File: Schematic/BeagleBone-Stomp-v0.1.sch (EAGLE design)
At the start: 53 parts, among them U1 MSP430G2553_RHB_32, U2 TLV320AIC3120_RHB_32, U3 TPS73701_DRB_8

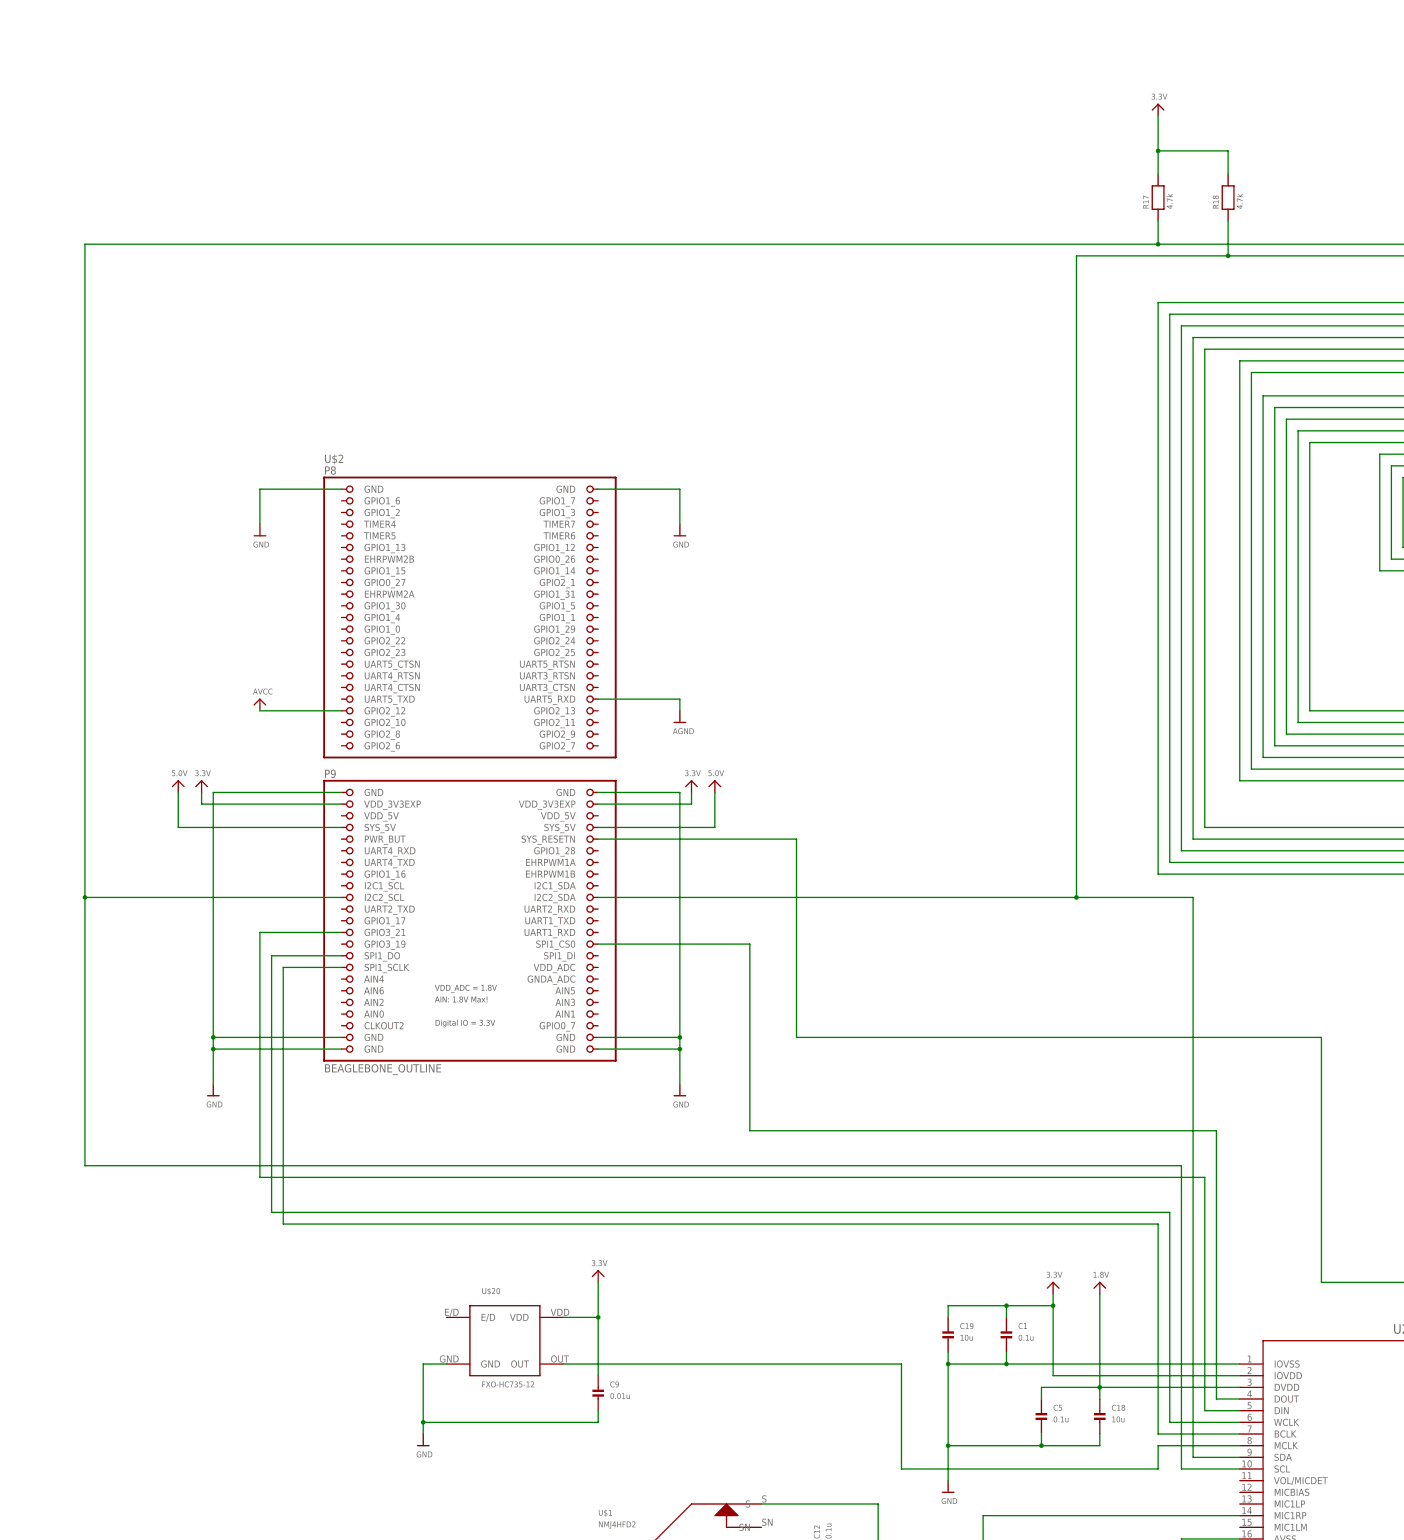
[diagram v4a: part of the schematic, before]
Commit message: Adding in EEPROM chip
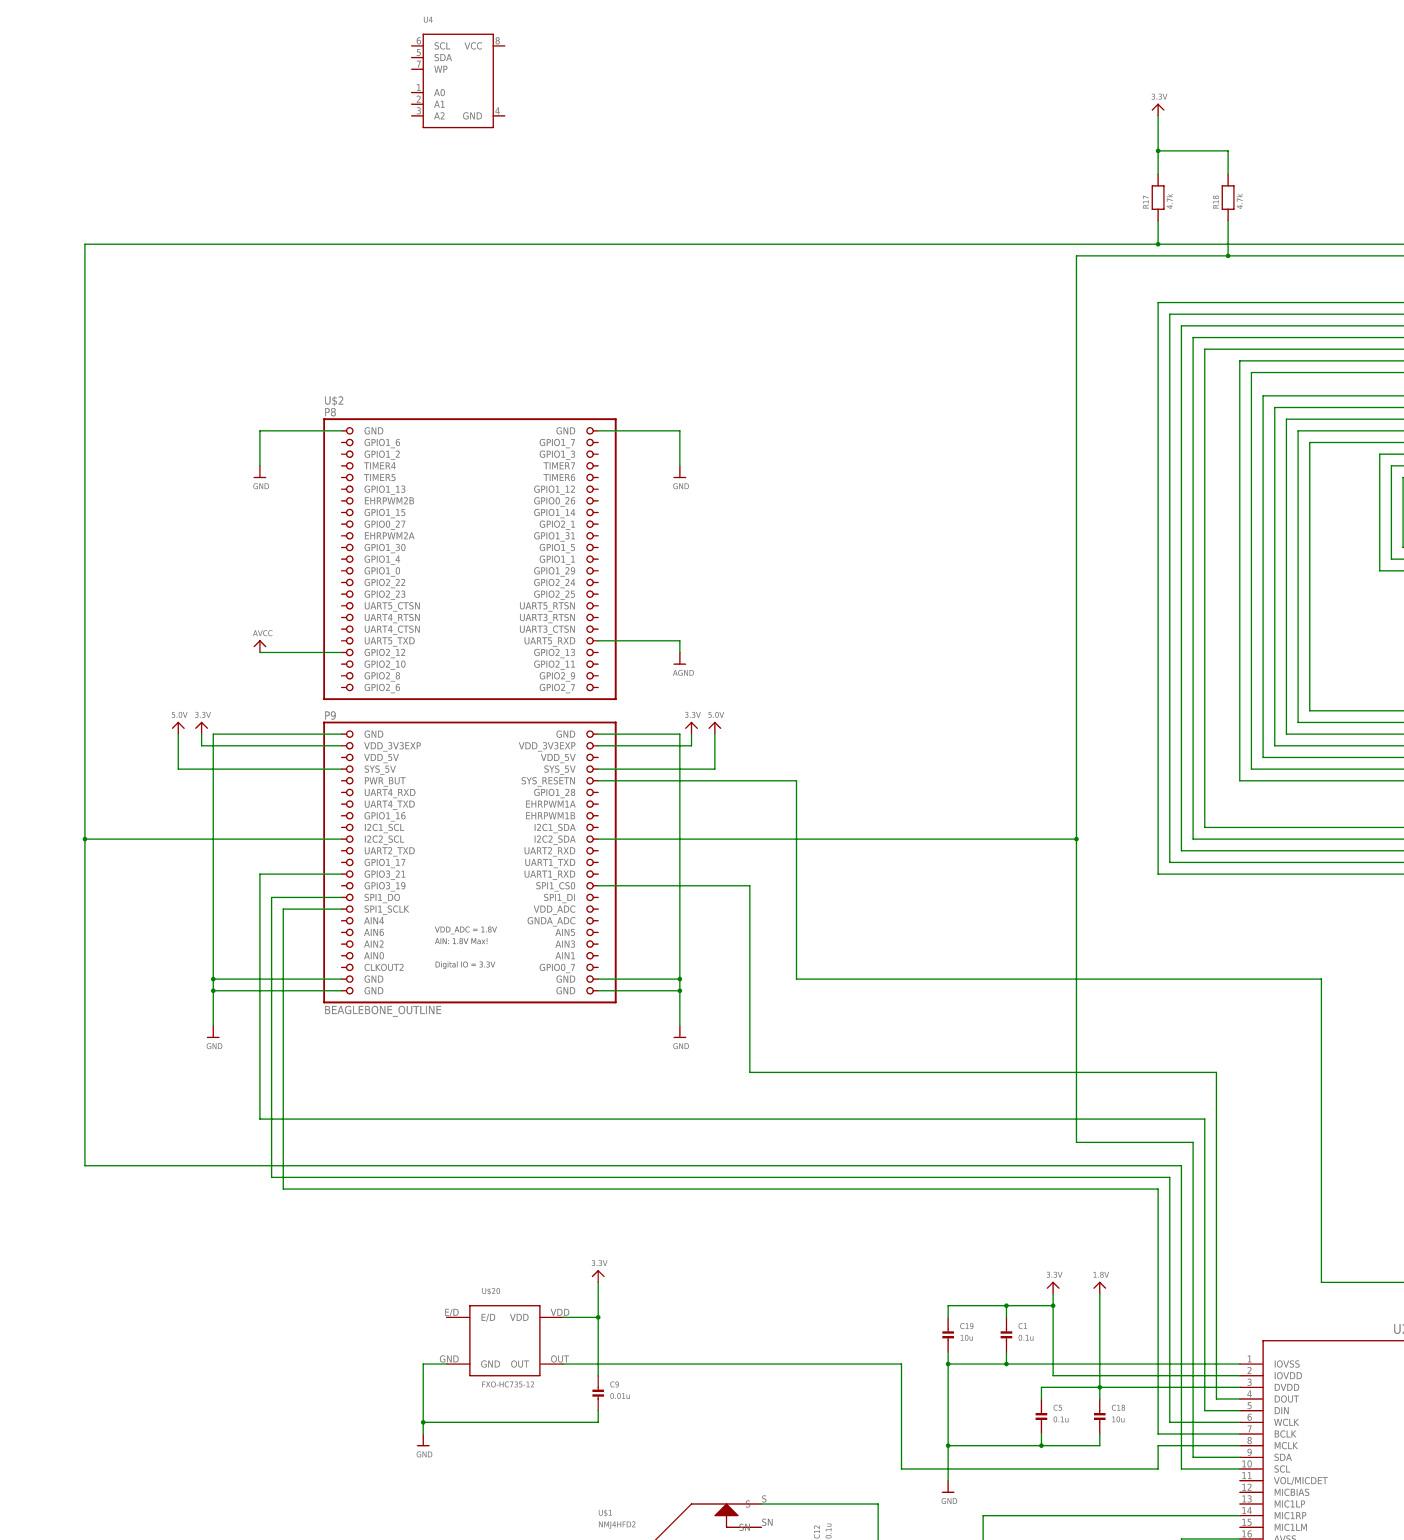
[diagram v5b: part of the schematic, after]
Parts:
- added U4: (no value), microbuilder:EEPROM_I2C_SOIC8_GENERIC
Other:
- moved on the sheet: U$2

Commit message: Pretty close to being done just need to check connections on schematic and make BOM
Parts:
- removed C13: 0.1u, microbuilder:CAP_CERAMIC0402
- added C11: 0.1u, microbuilder:CAP_CERAMIC0402
- added R19, R20, R21: 4.7k, microbuilder:RESISTOR0402
- added R22: 10k, microbuilder:RESISTOR0402
- added SW1: (no value), microbuilder:DIPSWITCH_2PIN
- R3, R4, R5, R6, R7, R8, R9: value 470 -> 100
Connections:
- removed net AVCC: U$2.GPIO2_12
- removed net N$17: JP2.1, U1.P1.5/TA0.0/UCB0CLK/UCA0STE/A5/CA5/TMS
- removed net N$19: JP2.4, U1.P1.2/TA0.1/UCA0TXD/UCA0SIMO/A2/CA2
- removed net N$20: JP2.5, U1.P1.1/TA0.0/UCA0RXD/UCA0SOMI/A1/CA1
- removed net N$21: JP2.3, U1.P1.3/ADC10CLK/CAOUT/VREF-/VEREF-/A3/CA3
- removed net N$24: U$2.GPIO3_21, U2.DIN
- removed net N$25: JP1.19, U1.P2.3/TA1.0
- removed net N$26: JP1.20, U1.P3.4/TA0.0
- removed net N$27: JP1.14, U1.P3.7/TA1CLK/CAOUT
- removed net N$28: JP1.15, U1.P3.6/TA0.2
- removed net N$29: JP1.16, U1.P3.5/TA0.1
- removed net N$30: JP1.17, U1.P2.5/TA1.2
- removed net N$31: JP1.18, U1.P2.4/TA1.2
- removed net N$34: JP2.7, R16.2, U1.P3.1/TA1.0
- removed net N$35: JP2.8, R15.2, U1.P3.0/TA0.2
- removed net N$36: JP2.9, R14.2, U1.P2.0/TA1.0
- removed net N$37: JP2.10, R13.2, U1.P2.1/TA1.1
- removed net N$38: JP2.11, R12.2, U1.P2.2/TA1.1
- removed net N$39: JP2.12, R11.2, U1.P3.2/TA1.1
- removed net N$40: JP2.13, R10.2, U1.P3.3/TA1.2
- removed net N$41: U$2.SPI1_DO, U2.WCLK
- removed net N$42: U$2.SPI1_SCLK, U2.BCLK
- removed net N$43: C16.P$1, C17.P$1, U2.SPKVDD_2
- removed net N$45: U$2.SYS_RESETN, U2.*RESET
- removed net N$46: R17.1, U$2.I2C2_SCL, U1.P1.6/TA0.1/UCB0SOMI/UCB0SCL/A6/CA6/TDI/TCLK, U2.SCL
- removed net N$47: R18.1, U$2.I2C2_SDA, U1.P1.7/CAOUT/UCB0SIMO/UCB0SDA/A7/CA7/TDO/TDI, U2.SDA
- removed net N$8 (its old number): U$20.OUT, U2.MCLK
- new net N$5: R19.1, SW1.1B, U4.A0
- new net P$1: JP1.14, JP1.15, JP1.16, JP1.17, JP1.18, JP1.19, JP1.20, JP2.1, JP2.10, JP2.11, JP2.12, JP2.13, JP2.2, JP2.3, JP2.4, JP2.5, JP2.6, JP2.7, JP2.8, JP2.9, R10.2, R11.2, R12.2, R13.2, R14.2, R15.2, R16.2, R17.1, R18.1, U$1.SN, U$1.TN, U$2.GPIO3_21, U$2.I2C2_SCL, U$2.I2C2_SDA, U$2.SPI1_CS0, U$2.SPI1_DO, U$2.SPI1_SCLK, U$2.SYS_RESETN, U$20.E/D, U$20.OUT, U$7.SN, U$7.TN, U1.NC, U1.NC_2, U1.P1.0/TA0CLK/ACLK/A0/CA0, U1.P1.1/TA0.0/UCA0RXD/UCA0SOMI/A1/CA1, U1.P1.2/TA0.1/UCA0TXD/UCA0SIMO/A2/CA2, U1.P1.3/ADC10CLK/CAOUT/VREF-/VEREF-/A3/CA3, U1.P1.4/SMCLK/UCB0STE/UCA0CLK/VREF+/VEREF+/A4/CA4/TCK, U1.P1.5/TA0.0/UCB0CLK/UCA0STE/A5/CA5/TMS, U1.P1.6/TA0.1/UCB0SOMI/UCB0SCL/A6/CA6/TDI/TCLK, U1.P1.7/CAOUT/UCB0SIMO/UCB0SDA/A7/CA7/TDO/TDI, U1.P2.0/TA1.0, U1.P2.1/TA1.1, U1.P2.2/TA1.1, U1.P2.3/TA1.0, U1.P2.4/TA1.2, U1.P2.5/TA1.2, U1.P3.0/TA0.2, U1.P3.1/TA1.0, U1.P3.2/TA1.1, U1.P3.3/TA1.2, U1.P3.4/TA0.0, U1.P3.5/TA0.1, U1.P3.6/TA0.2, U1.P3.7/TA1CLK/CAOUT, U1.XIN/P2.6/TA0.1, U1.XOUT/P2.7, U2.*RESET, U2.BCLK, U2.DIN, U2.DOUT, U2.GPIO1, U2.MCLK, U2.MIC1LM, U2.MIC1LP, U2.MICBIAS, U2.NC, U2.SCL, U2.SDA, U2.VOL/MICDET, U2.WCLK, U3.NC, U3.NC_2, U3.NC_3, U4.SCL, U4.SDA
- net 3.3V: now also C11.P$1, R19.2, R20.2, R21.2, R22.2, U4.VCC; no longer C13.P$1
- net 5.0V: now also C16.P$1, C17.P$1, U2.SPKVDD_2
- net AGND: no longer C13.P$2, U$2.UART5_RXD, U1.AVSS, U1.EPAD
- net GND: now also C11.P$2, SW1.1A, SW1.2A, U1.AVSS, U1.EPAD, U4.GND
- net N$11: now also R20.1, SW1.2B, U4.A1; no longer U$2.SPI1_CS0, U2.DOUT
- net N$12: now also R21.1, U4.A2; no longer JP2.6, U1.P1.0/TA0CLK/ACLK/A0/CA0
- net N$18: now also R22.1, U4.WP; no longer JP2.2, U1.P1.4/SMCLK/UCB0STE/UCA0CLK/VREF+/VEREF+/A4/CA4/TCK
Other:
- moved on the sheet: C1, C10, C12, C14, C15, C16, C17, C18, C19, C2, C3, C4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

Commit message: Removing arrows and such
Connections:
- removed net P$1: JP1.14, JP1.15, JP1.16, JP1.17, JP1.18, JP1.19, JP1.20, JP2.1, JP2.10, JP2.11, JP2.12, JP2.13, JP2.2, JP2.3, JP2.4, JP2.5, JP2.6, JP2.7, JP2.8, JP2.9, R10.2, R11.2, R12.2, R13.2, R14.2, R15.2, R16.2, R17.1, R18.1, U$1.SN, U$1.TN, U$2.GPIO3_21, U$2.I2C2_SCL, U$2.I2C2_SDA, U$2.SPI1_CS0, U$2.SPI1_DO, U$2.SPI1_SCLK, U$2.SYS_RESETN, U$20.E/D, U$20.OUT, U$7.SN, U$7.TN, U1.NC, U1.NC_2, U1.P1.0/TA0CLK/ACLK/A0/CA0, U1.P1.1/TA0.0/UCA0RXD/UCA0SOMI/A1/CA1, U1.P1.2/TA0.1/UCA0TXD/UCA0SIMO/A2/CA2, U1.P1.3/ADC10CLK/CAOUT/VREF-/VEREF-/A3/CA3, U1.P1.4/SMCLK/UCB0STE/UCA0CLK/VREF+/VEREF+/A4/CA4/TCK, U1.P1.5/TA0.0/UCB0CLK/UCA0STE/A5/CA5/TMS, U1.P1.6/TA0.1/UCB0SOMI/UCB0SCL/A6/CA6/TDI/TCLK, U1.P1.7/CAOUT/UCB0SIMO/UCB0SDA/A7/CA7/TDO/TDI, U1.P2.0/TA1.0, U1.P2.1/TA1.1, U1.P2.2/TA1.1, U1.P2.3/TA1.0, U1.P2.4/TA1.2, U1.P2.5/TA1.2, U1.P3.0/TA0.2, U1.P3.1/TA1.0, U1.P3.2/TA1.1, U1.P3.3/TA1.2, U1.P3.4/TA0.0, U1.P3.5/TA0.1, U1.P3.6/TA0.2, U1.P3.7/TA1CLK/CAOUT, U1.XIN/P2.6/TA0.1, U1.XOUT/P2.7, U2.*RESET, U2.BCLK, U2.DIN, U2.DOUT, U2.GPIO1, U2.MCLK, U2.MIC1LM, U2.MIC1LP, U2.MICBIAS, U2.NC, U2.SCL, U2.SDA, U2.VOL/MICDET, U2.WCLK, U3.NC, U3.NC_2, U3.NC_3, U4.SCL, U4.SDA
- new net CODEC_BCLK: U$2.SPI1_SCLK, U2.BCLK
- new net CODEC_DIN: U$2.GPIO3_21, U2.DIN
- new net CODEC_DOUT: U$2.SPI1_CS0, U2.DOUT
- new net CODEC_MCLK: U$20.OUT, U2.MCLK
- new net CODEC_WCLK: U$2.SPI1_DO, U2.WCLK
- new net I2C_CLK: R17.1, U$2.I2C2_SCL, U1.P1.6/TA0.1/UCB0SOMI/UCB0SCL/A6/CA6/TDI/TCLK, U2.SCL, U4.SCL
- new net I2C_DATA: R18.1, U$2.I2C2_SDA, U1.P1.7/CAOUT/UCB0SIMO/UCB0SDA/A7/CA7/TDO/TDI, U2.SDA, U4.SDA
- new net LED1: JP1.14, U1.P3.4/TA0.0
- new net LED2: JP1.15, U1.P2.3/TA1.0
- new net LED3: JP1.16, U1.P2.4/TA1.2
- new net LED4: JP1.17, U1.P2.5/TA1.2
- new net LED5: JP1.18, U1.P3.5/TA0.1
- new net LED6: JP1.19, U1.P3.6/TA0.2
- new net LED7: JP1.20, U1.P3.7/TA1CLK/CAOUT
- new net POT1: JP2.1, U1.P1.0/TA0CLK/ACLK/A0/CA0
- new net POT2: JP2.2, U1.P1.1/TA0.0/UCA0RXD/UCA0SOMI/A1/CA1
- new net POT3: JP2.3, U1.P1.2/TA0.1/UCA0TXD/UCA0SIMO/A2/CA2
- new net POT4: JP2.4, U1.P1.3/ADC10CLK/CAOUT/VREF-/VEREF-/A3/CA3
- new net POT5: JP2.5, U1.P1.4/SMCLK/UCB0STE/UCA0CLK/VREF+/VEREF+/A4/CA4/TCK
- new net POT6: JP2.6, U1.P1.5/TA0.0/UCB0CLK/UCA0STE/A5/CA5/TMS
- new net RESET: U$2.SYS_RESETN, U2.*RESET
- new net STOMP1: JP2.7, R16.2, U1.P3.1/TA1.0
- new net STOMP2: JP2.8, R15.2, U1.P3.0/TA0.2
- new net STOMP3: JP2.9, R14.2, U1.P2.0/TA1.0
- new net STOMP4: JP2.10, R13.2, U1.P2.1/TA1.1
- new net STOMP5: JP2.11, R12.2, U1.P2.2/TA1.1
- new net STOMP6: JP2.12, R11.2, U1.P3.2/TA1.1
- new net STOMP7: JP2.13, R10.2, U1.P3.3/TA1.2
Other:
- moved on the sheet: C11, C14, GND, R17, R18, R19, R20, R21, R22, RST, SW1, TST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

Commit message: Cleaning libraries up
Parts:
- removed GND, RST, TST, VCC: WIREPAD2,15/1,0, wirepad:WIREPAD2,15/1,0
- removed SW1: (no value), microbuilder:DIPSWITCH_2PIN
- removed U$1, U$7: NMJ4HFD2, bone:NMJ4HFD2
- removed U$2: BEAGLEBONE_OUTLINE, microbuilder:BEAGLEBONE_OUTLINE
- removed U$20: FXO-HC735-12, bone:FXO-HC735-12
- added C13: 2.2u, microbuilder:CAP_CERAMIC0402
- added J1: (no value), bone:TC2030-MCP
- added J2, J3: NMJ4HFD2, bone:NMJ4HFD2
- added R23: 47k, microbuilder:RESISTOR0402
- added S1: CTS-219-2MST, bone:CTS-219-2MST
- added U$5: BEAGLEBONE_OUTLINE, bone:BEAGLEBONE_OUTLINE
- added U5: FXO-HC735-12, bone:FXO-HC735-12
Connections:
- net 3.3V: now also J1.VCC_IN, R23.2, U$5.VDD_3V3EXP@1, U$5.VDD_3V3EXP@2, U5.VDD; no longer U$2.VDD_3V3EXP@1, U$2.VDD_3V3EXP@2, U$20.VDD, VCC.P
- net 5.0V: now also U$5.SYS_5V@1, U$5.SYS_5V@2; no longer U$2.SYS_5V@1, U$2.SYS_5V@2
- net AGND: now also J2.S, J3.S; no longer U$1.S, U$7.S
- net CODEC_BCLK: now also U$5.SPI1_SCLK; no longer U$2.SPI1_SCLK
- net CODEC_DIN: now also U$5.GPIO3_21; no longer U$2.GPIO3_21
- net CODEC_DOUT: now also U$5.SPI1_CS0; no longer U$2.SPI1_CS0
- net CODEC_MCLK: now also U5.OUT; no longer U$20.OUT
- net CODEC_WCLK: now also U$5.SPI1_DO; no longer U$2.SPI1_DO
- net GND: now also C13.P$2, J1.VSS, S1.P$1, S1.P$2, U$5.GND@1, U$5.GND@2, U$5.GND@3, U$5.GND@4, U$5.GND@5, U$5.GND@6, U$5.GND@7, U$5.GND@8, U5.GND; no longer GND.P, SW1.1A, SW1.2A, U$2.GND@1, U$2.GND@2, U$2.GND@3, U$2.GND@4, U$2.GND@5, U$2.GND@6, U$2.GND@7, U$2.GND@8, U$20.GND
- net I2C_CLK: now also U$5.I2C2_SCL; no longer U$2.I2C2_SCL
- net I2C_DATA: now also U$5.I2C2_SDA; no longer U$2.I2C2_SDA
- net N$11: now also S1.P$3; no longer SW1.2B
- net N$32: now also J1.SBWTCK; no longer TST.P
- net N$33: now also C13.P$1, J1.SBWTDIO, R23.1; no longer RST.P
- net N$5: now also S1.P$4; no longer SW1.1B
- net N$6: now also J3.T; no longer U$7.T
- net N$9: now also J2.T; no longer U$1.T
- net RESET: now also U$5.SYS_RESETN; no longer U$2.SYS_RESETN
